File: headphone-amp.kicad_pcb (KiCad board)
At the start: 2 copper layers, 61.5 x 20 mm, 21 parts, among them J1 AudioJack4, J2 AudioJack4, J3 Conn_01x02_Male, SW1 SW_SPDT, U1 RC4580, U2 TMA0512D

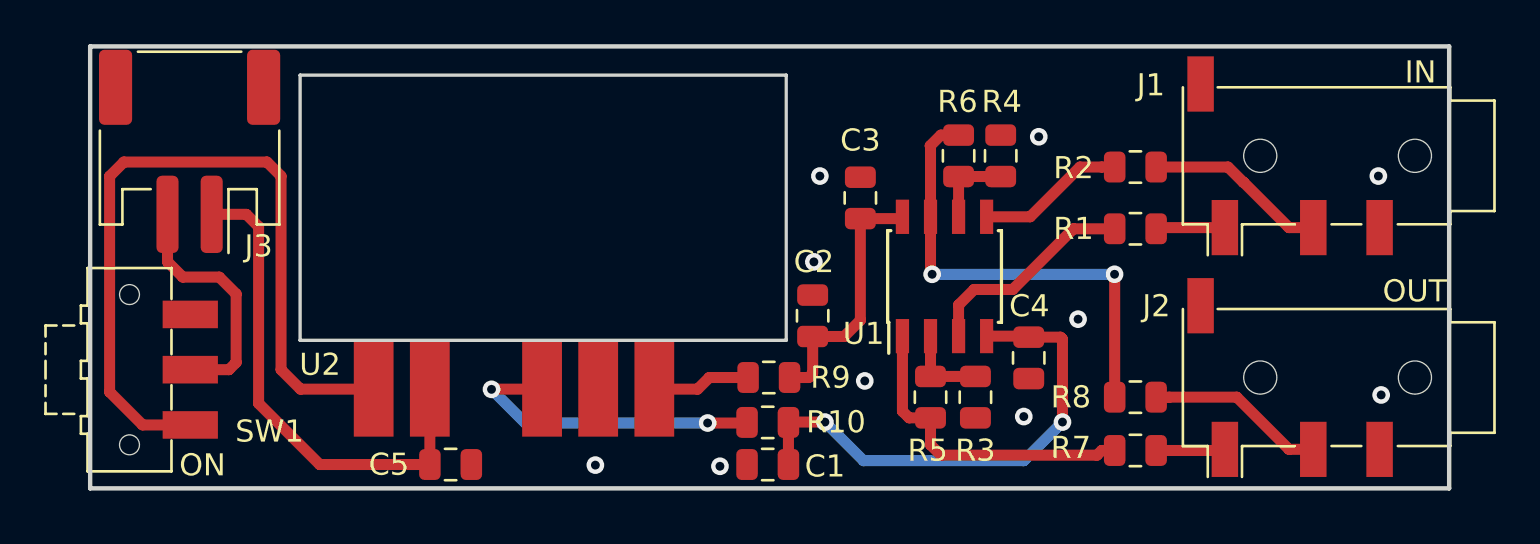
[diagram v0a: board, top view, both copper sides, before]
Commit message: changed feedback networks slightly
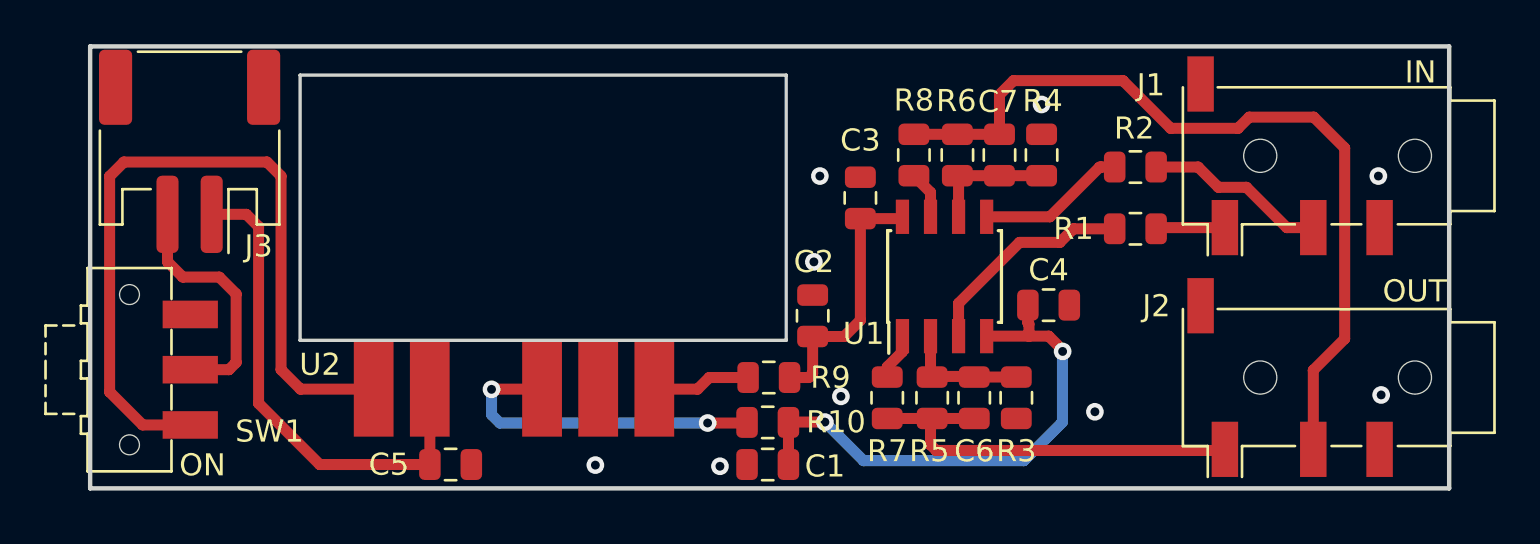
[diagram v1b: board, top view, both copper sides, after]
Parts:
- added C6: 22p, Capacitor_SMD:C_0805_2012Metric, F.Cu at (119.5, 88.9)
- added C7: 22p, Capacitor_SMD:C_0805_2012Metric, F.Cu at (120.7, 77.9)
- moved R8 14.9 mm to (116.8, 77.9), turned to 90 degrees
- moved R7 11.5 mm to (115.6, 88.9), turned to 270 degrees
- moved C4 2.55 mm to (122.9, 84.7), turned to 180 degrees
- moved R4 1.85 mm to (122.6, 77.9)
- moved R3 1.85 mm to (121.4, 88.9)
- moved R5 0.08 mm to (117.6, 88.9)
- moved R6 0.07 mm to (118.7, 77.9)
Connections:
- R5 pad 2: Net-(R5-Pad2) -> /Left_out
- R6 pad 2: Net-(R6-Pad2) -> /Right_out
- R7 pad 1: Net-(R5-Pad2) -> Net-(R7-Pad1)
- R8 pad 1: Net-(R6-Pad2) -> Net-(R8-Pad1)
- U1 pad 1: Net-(R5-Pad2) -> Net-(R7-Pad1)
- U1 pad 7: Net-(R6-Pad2) -> Net-(R8-Pad1)
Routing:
- net /Right_out: track 8.09 -> 37.5 mm
- net Net-(R6-Pad2): track 21.2 -> 0.00 mm, vias 2 -> 0
- net /Left_out: track 3.13 -> 18.6 mm
- net Net-(R5-Pad2): track 14.6 -> 0.00 mm
- net Net-(R8-Pad1): track 0.00 -> 2.17 mm
- net Net-(R7-Pad1): track 0.00 -> 2.14 mm
- net Net-(C7-Pad2): track 3.73 -> 5.63 mm
- net Net-(C6-Pad2): track 3.86 -> 5.76 mm
- net -12V: track 23.0 -> 24.1 mm
- net Net-(R10-Pad2): track 14.5 -> 15.2 mm
- net GND: vias 10 -> 9

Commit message: tag for prototype production
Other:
- board text added: "5V Headphone Amplifier Designed by Joe Earlam Rev: p1"
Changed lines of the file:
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@@
-(kicad_pcb (version 20171130) (host pcbnew "(5.0.2)-1")
+(kicad_pcb (version 20171130) (host pcbnew 5.0.2-bee76a0~70~ubuntu16.04.1)
   (general
     (thickness 1.6)
-    (drawings 7)
+    (drawings 8)
     (tracks 118)
     (zones 0)
@@
   )
   (setup
-    (last_trace_width 0.5)
+    (last_trace_width 0.25)
     (user_trace_width 0.5)
     (trace_clearance 0.2)
@@
     (visible_elements 7FFFFFFF)
     (pcbplotparams
-      (layerselection 0x010fc_ffffffff)
-      (usegerberextensions false)
+      (layerselection 0x010f0_ffffffff)
+      (usegerberextensions true)
       (usegerberattributes false)
       (usegerberadvancedattributes false)
@@
       (outputformat 1)
       (mirror false)
-      (drillshape 1)
+      (drillshape 0)
       (scaleselection 1)
-      (outputdirectory ""))
+      (outputdirectory "../../../../gerbers/headphone/"))
   )
   (net 0 "")
@@
     )
   )
+  (gr_text "5V Headphone Amplifier\nDesigned by Joe Earlam\nRev: p1" (at 140.462 82.931) (layer B.SilkS)
+    (effects (font (size 1.5 1.5) (thickness 0.3)) (justify left mirror))
+  )
   (gr_text ON (at 84.582 91.948) (layer F.SilkS)
     (effects (font (size 1 1) (thickness 0.2)))
@@
   (via (at 113.4745 88.8365) (size 0.8) (drill 0.4) (layers F.Cu B.Cu) (net 5))
   (via (at 124.968 89.535) (size 0.8) (drill 0.4) (layers F.Cu B.Cu) (net 5))
-  (segment (start 117.529 86.112) (end 117.529 87.9355) (width 0.5) (layer F.Cu) (net 19))
-  (segment (start 117.529 87.9355) (end 119.561 87.9355) (width 0.5) (layer F.Cu) (net 19))
-  (segment (start 118.799 78.8885) (end 118.799 80.712) (width 0.5) (layer F.Cu) (net 18))
   (segment (start 117.529 91.029) (end 117.529 89.8105) (width 0.5) (layer F.Cu) (net 6))
   (segment (start 117.786 91.286) (end 117.529 91.029) (width 0.5) (layer F.Cu) (net 6))
@@
   (segment (start 83 82.746) (end 83 80.6) (width 0.5) (layer F.Cu) (net 16))
   (segment (start 83.693 83.439) (end 83 82.746) (width 0.5) (layer F.Cu) (net 16))
+  (segment (start 118.799 78.8885) (end 118.799 80.712) (width 0.5) (layer F.Cu) (net 18))
   (segment (start 122.555 78.852) (end 120.65 78.852) (width 0.5) (layer F.Cu) (net 18))
   (segment (start 118.745 78.852) (end 120.65 78.852) (width 0.5) (layer F.Cu) (net 18))
+  (segment (start 117.529 86.112) (end 117.529 87.9355) (width 0.5) (layer F.Cu) (net 19))
+  (segment (start 117.529 87.9355) (end 119.561 87.9355) (width 0.5) (layer F.Cu) (net 19))
   (segment (start 121.412 87.9625) (end 119.507 87.9625) (width 0.5) (layer F.Cu) (net 19))
   (segment (start 117.529 79.6045) (end 117.529 80.712) (width 0.5) (layer F.Cu) (net 20))

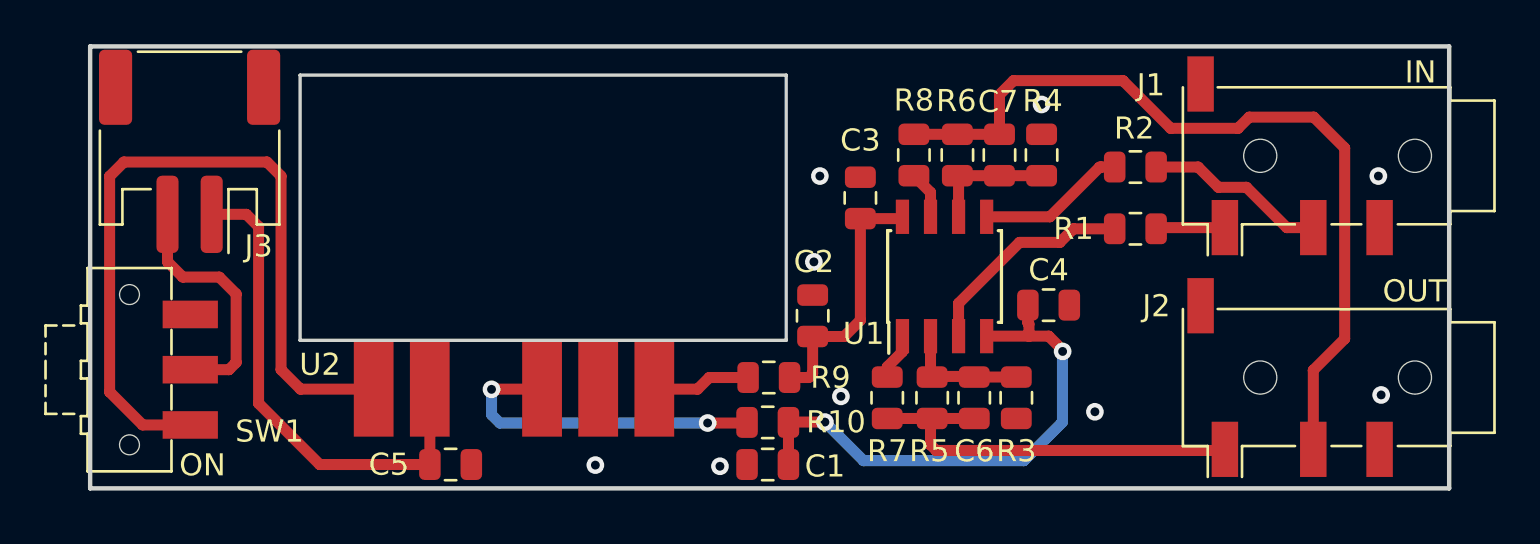
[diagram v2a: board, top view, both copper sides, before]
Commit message: changed filtering network
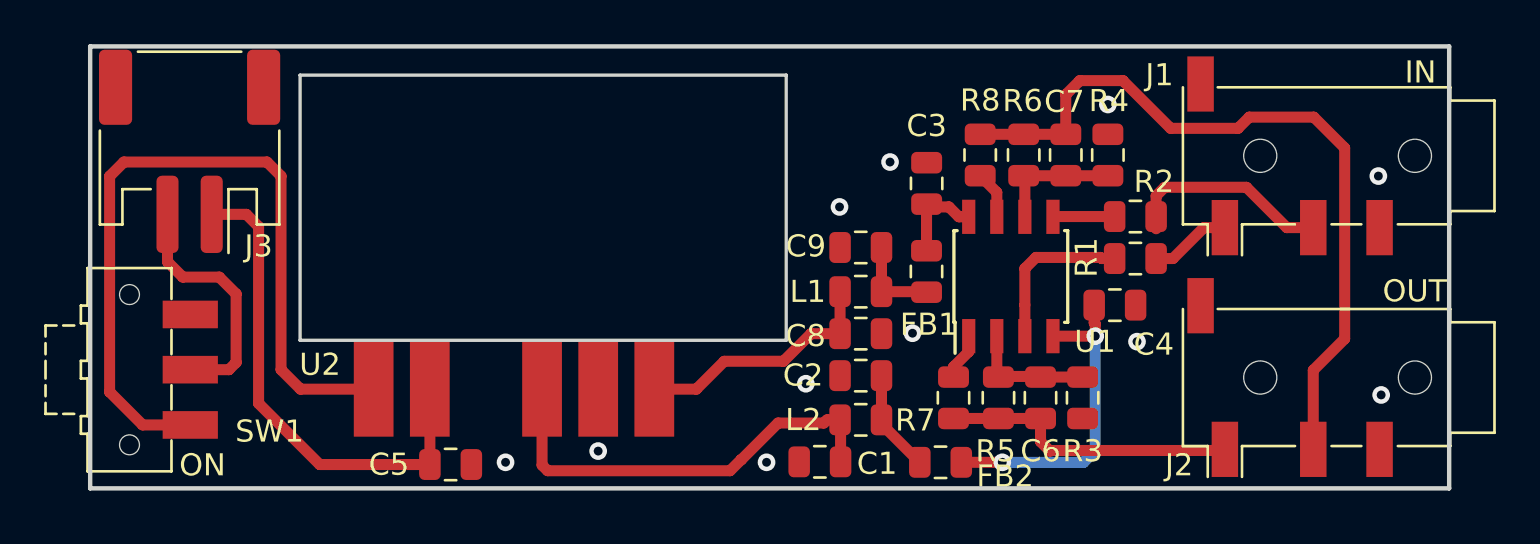
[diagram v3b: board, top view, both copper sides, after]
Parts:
- removed R10, R9: 10R, Resistor_SMD:R_0805_2012Metric
- added C8: 10u, Capacitor_SMD:C_0805_2012Metric, F.Cu at (114.4, 86.0)
- added C9: 10u, Capacitor_SMD:C_0805_2012Metric, F.Cu at (114.4, 82.1)
- added FB1: FB, Inductor_SMD:L_0805_2012Metric, F.Cu at (117.3, 83.2)
- added FB2: FB, Inductor_SMD:L_0805_2012Metric, F.Cu at (118.0, 91.8)
- added L1: 10u, Inductor_SMD:L_0805_2012Metric, F.Cu at (114.4, 84.1)
- added L2: 10u, Inductor_SMD:L_0805_2012Metric, F.Cu at (114.4, 89.9)
- moved C2 3.48 mm to (114.4, 87.9), turned to 180 degrees
- moved C3 3.07 mm to (117.4, 79.2)
- moved C4 3.00 mm to (125.9, 84.7)
- moved C6 3.00 mm to (122.5, 88.9)
- moved C7 3.00 mm to (123.7, 77.9)
- moved R3 3.00 mm to (124.4, 88.9)
- moved R4 3.00 mm to (125.6, 77.9)
- moved R5 3.00 mm to (120.6, 88.9)
- moved R6 3.00 mm to (121.7, 77.9)
- moved R7 3.00 mm to (118.6, 88.9)
- moved R8 3.00 mm to (119.8, 77.9)
- moved U1 3.00 mm to (121.2, 83.4)
- moved C1 2.36 mm to (112.5, 91.8)
- moved R2 2.24 mm to (126.8, 80.7)
- moved R1 1.35 mm to (126.8, 82.6)
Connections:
- C1 pad 1: -12V -> Net-(C1-Pad1)
- C2 pad 1: +12V -> Net-(C2-Pad1)
- U2 pad 4: Net-(R10-Pad2) -> Net-(C1-Pad1)
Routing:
- net Net-(C1-Pad1): track 0.00 -> 19.9 mm
- net Net-(R10-Pad2): track 15.2 -> 0.00 mm, vias 2 -> 0
- net -12V: track 24.1 -> 14.8 mm
- net +12V: track 11.8 -> 4.37 mm
- net Net-(C8-Pad1): track 4.46 -> 11.3 mm
- net /Left_out: track 18.6 -> 13.5 mm
- net Net-(C2-Pad1): track 0.00 -> 4.64 mm
- net Net-(C9-Pad1): track 0.00 -> 4.05 mm
- net Net-(R2-Pad1): track 6.77 -> 2.85 mm
- net /Right_out: track 37.5 -> 34.5 mm
- net Net-(R1-Pad1): track 9.95 -> 7.35 mm
- net /Right_in: track 8.25 -> 9.04 mm
- net /Left_in: track 3.13 -> 3.69 mm
- net GND: vias 9 -> 11
